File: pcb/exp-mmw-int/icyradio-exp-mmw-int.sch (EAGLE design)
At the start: 309 parts, among them Q1 AO3400, Q2 AO3400, U1 EFM32GG11B420F2048GQ64, U10 BFCV-2895+, U11 QCN-34+, U12 ADMV1013, U13 BFCV-2895+, U14 QCN-34+, U15 ADMV1014, U16 PMA2-123LN+, U17 ADRF5720, U18 PMA2-123LN+, U19 LTC5597, U2 MCP9802-A0, U20 ADRF5019, U21 ADRF5019, U22 LTC5597, U23 ADRF5019, U24 ADRF5019, U25 8V97003, U26 ADP7142AUJZ-3.3, U27 ADM7170ACPZ-5.0, U28 ADM7172ACPZ-3.3, U29 ADM8828, U3 MCP9802-A1, U30 ADP7142AUJZ-1.8, U31 ADP7142AUJZ-1.8, U32 ADP7102ACPZ-1.5, U33 ADM7171ACPZ-3.3, U34 ADM7171ACPZ-3.3, U4 MCP9802-A3, U5 FXL4TD245BQX, U6 FXL4TD245BQX, U7 MCP6V32-E/MNY, U8 MCP4728-A0, U9 MCP6V32-E/MNY

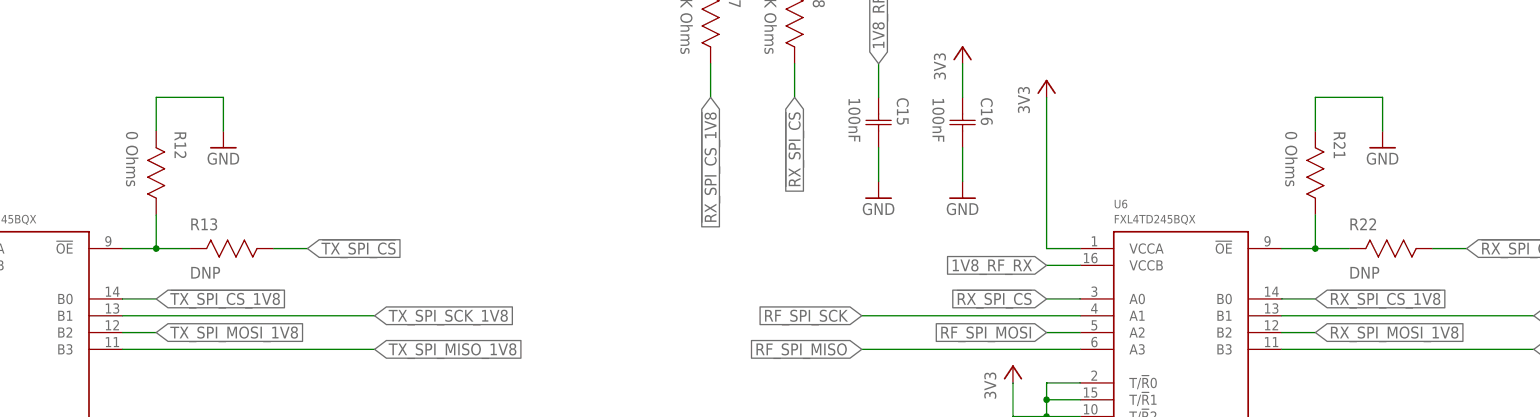
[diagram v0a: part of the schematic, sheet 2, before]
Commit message: pcb: Minor mmWave board schematic changes
Signed-off-by: João Silva <jgc3silva@gmail.com>
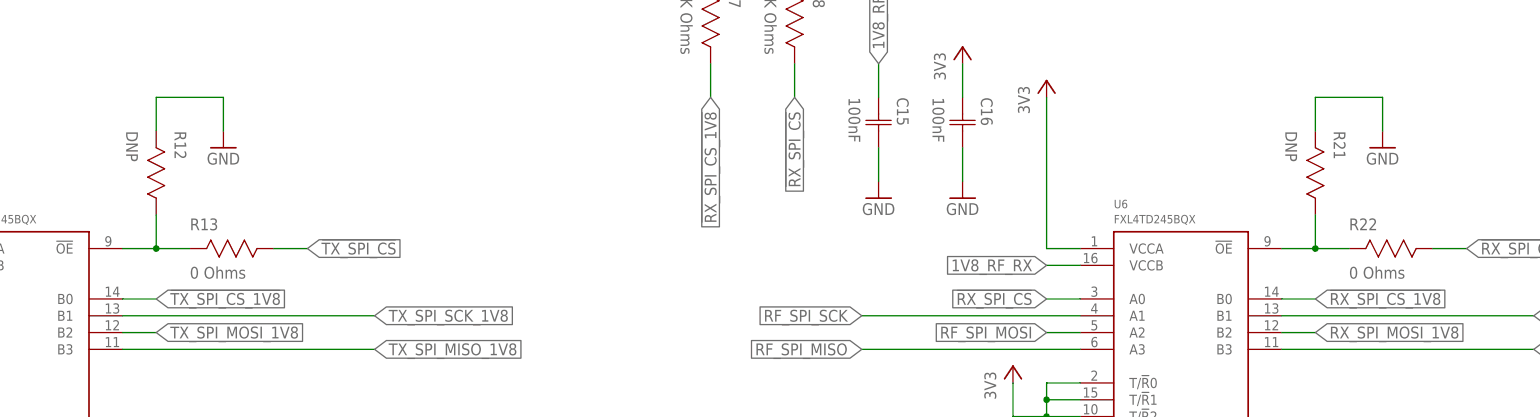
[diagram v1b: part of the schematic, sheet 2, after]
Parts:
- R12, R21: value 0 Ohms -> DNP
- R13, R22: value DNP -> 0 Ohms
- R69, R70: SERIES (none) -> FC0402
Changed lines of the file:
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@@
 <part name="3V21" library="Supply Symbol" deviceset="3V3" device=""/>
 <part name="3V22" library="Supply Symbol" deviceset="3V3" device=""/>
-<part name="R22" library="Resistor" deviceset="RESISTOR" device="-0402" value="DNP"/>
-<part name="R21" library="Resistor" deviceset="RESISTOR" device="-0402" value="0 Ohms"/>
+<part name="R22" library="Resistor" deviceset="RESISTOR" device="-0402" value="0 Ohms"/>
+<part name="R21" library="Resistor" deviceset="RESISTOR" device="-0402" value="DNP"/>
 <part name="R17" library="Resistor" deviceset="RESISTOR" device="-0402" value="10K Ohms"/>
 <part name="GND40" library="Supply Symbol" deviceset="GND" device=""/>
@@
 <attribute name="SERIES" value="ATC520L"/>
 </part>
-<part name="R70" library="Resistor" deviceset="RESISTOR" device="-0402" value="50 Ohms"/>
+<part name="R70" library="Resistor" deviceset="RESISTOR" device="-0402" value="50 Ohms">
+<attribute name="SERIES" value="FC0402"/>
+</part>
 <part name="GND428" library="Supply Symbol" deviceset="GND" device=""/>
 <part name="C126" library="Capacitor" deviceset="CAPACITOR" device="-0402" value="10nF">
 <attribute name="SERIES" value="ATC520L"/>
 </part>
-<part name="R69" library="Resistor" deviceset="RESISTOR" device="-0402" value="50 Ohms"/>
+<part name="R69" library="Resistor" deviceset="RESISTOR" device="-0402" value="50 Ohms">
+<attribute name="SERIES" value="FC0402"/>
+</part>
 <part name="GND429" library="Supply Symbol" deviceset="GND" device=""/>
 <part name="C124" library="Capacitor" deviceset="CAPACITOR" device="-0402" value="10nF">
@@
 <part name="GND215" library="Supply Symbol" deviceset="GND" device=""/>
 <part name="GND216" library="Supply Symbol" deviceset="GND" device=""/>
-<part name="R13" library="Resistor" deviceset="RESISTOR" device="-0402" value="DNP"/>
-<part name="R12" library="Resistor" deviceset="RESISTOR" device="-0402" value="0 Ohms"/>
+<part name="R13" library="Resistor" deviceset="RESISTOR" device="-0402" value="0 Ohms"/>
+<part name="R12" library="Resistor" deviceset="RESISTOR" device="-0402" value="DNP"/>
 <part name="U2" library="Microchip" deviceset="MCP9802-A*" device="" technology="0"/>
 <part name="U3" library="Microchip" deviceset="MCP9802-A*" device="" technology="1"/>
@@
 <attribute name="NAME" x="327.8886" y="124.46" size="1.778" layer="95" ratio="10" rot="SR270"/>
 <attribute name="TOLERANCE" x="319.8114" y="124.46" size="1.778" layer="97" ratio="10" rot="SR270" align="top-left"/>
+<attribute name="SERIES" x="325.12" y="124.46" size="1.778" layer="96" rot="R270" display="off"/>
 </instance>
 <instance part="GND428" gate="G$1" x="325.12" y="106.68" smashed="yes">
@@
 <attribute name="NAME" x="327.8886" y="175.26" size="1.778" layer="95" ratio="10" rot="SR270"/>
 <attribute name="TOLERANCE" x="319.8114" y="175.26" size="1.778" layer="97" ratio="10" rot="SR270" align="top-left"/>
+<attribute name="SERIES" x="325.12" y="175.26" size="1.778" layer="96" rot="R270" display="off"/>
 </instance>
 <instance part="GND429" gate="G$1" x="325.12" y="157.48" smashed="yes">
